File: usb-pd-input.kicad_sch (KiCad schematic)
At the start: 18 parts, among them J1 USB-C, J2 Pogo pads, Q1 -30V -4A, U1 STUSB4500QTR

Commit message: fix: Add missing footprints and LCSC Part numbers to R15, R16, J2
R15/R16: footprint zudo-pd:R0603, LCSC Part C25999 (4.7k 0603 Basic)
J2: footprint zudo-pd:PogoPad_1x04_P2.54mm (no LCSC, bare copper pads)

Co-Authored-By: Claude <noreply@anthropic.com>
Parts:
- J2: footprint (none) -> zudo-pd:PogoPad_1x04_P2.54mm
- R15, R16: footprint (none) -> zudo-pd:R0603; LCSC Part (none) -> C25999
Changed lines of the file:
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@@
 			)
 		)
-		(property "Footprint" ""
+		(property "Footprint" "zudo-pd:PogoPad_1x04_P2.54mm"
 			(at 120.65 127 0)
 			(effects
@@
 			)
 		)
-		(property "Footprint" ""
+		(property "Footprint" "zudo-pd:R0603"
 			(at 126.492 135.89 90)
 			(effects
@@
 		)
 		(property "Description" "Resistor"
+			(at 128.27 135.89 0)
+			(effects
+				(font
+					(size 1.27 1.27)
+				)
+				(hide yes)
+			)
+		)
+		(property "LCSC Part" "C25999"
 			(at 128.27 135.89 0)
 			(effects
@@
 			)
 		)
-		(property "Footprint" ""
+		(property "Footprint" "zudo-pd:R0603"
 			(at 136.652 135.89 90)
 			(effects
@@
 			(at 138.43 135.89 0)
 			(effects
+				(font
+					(size 1.27 1.27)
+				)
+				(hide yes)
+			)
+		)
+		(property "LCSC Part" "C25999"
+			(at 138.43 135.89 0)
+			(effects

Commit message: refactor(hardware): update LCSC part numbers and PCB routing for PCBA v2
- Update capacitor part numbers to JLCPCB-compatible variants
- Standardize LCSC part property naming across schematics
- Adjust PCB routing for improved layout and signal integrity

Co-Authored-By: Claude <noreply@anthropic.com>
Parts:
- C1: LCSC Part C7432781 -> C13585
- C2, C35: LCSC Part C49678 -> C28233
- C30, C34: LCSC Part C6119849 -> C15849
- R11: LCSC Part C14675 -> C25803
- R12: LCSC Part C23168 -> C23206
- R15, R16: LCSC Part C25999 -> C23162
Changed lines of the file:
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@@
 			)
 		)
-		(property "LCSC Part" "C14675"
+		(property "LCSC Part" "C25803"
 			(at 200.66 104.14 0)
 			(effects
@@
 			)
 		)
-		(property "Datasheet" "https://lcsc.com/product-detail/Multilayer-Ceramic-Capacitors-MLCC-SMD-SMT_100nF-104-10-50V_C49678.html"
+		(property "Datasheet" "https://jlcpcb.com/partdetail/C28233"
 			(at 203.2 115.57 0)
 			(effects
@@
 			)
 		)
-		(property "LCSC Part" "C49678"
+		(property "LCSC Part" "C28233"
 			(at 200.66 115.57 0)
 			(effects
@@
 			)
 		)
-		(property "LCSC Part" "C7432781"
+		(property "LCSC Part" "C13585"
 			(at 243.84 21.59 0)
 			(effects
@@
 			)
 		)
-		(property "Datasheet" "https://lcsc.com/product-detail/Multilayer-Ceramic-Capacitors-MLCC-SMD-SMT_100nF-104-10-50V_C49678.html"
+		(property "Datasheet" "https://jlcpcb.com/partdetail/C28233"
 			(at 227.33 21.59 0)
 			(effects
@@
 			)
 		)
-		(property "LCSC Part" "C49678"
+		(property "LCSC Part" "C28233"
 			(at 229.87 21.59 0)
 			(effects
@@
 			)
 		)
-		(property "LCSC Part" "C6119849"
+		(property "LCSC Part" "C15849"
 			(at 217.17 46.99 0)
 			(effects
@@
 			)
 		)
-		(property "LCSC Part" "C25999"
+		(property "LCSC Part" "C23162"
 			(at 128.27 135.89 0)
 			(effects
@@
 			)
 		)
-		(property "LCSC Part" "C25999"
+		(property "LCSC Part" "C23162"
 			(at 138.43 135.89 0)
 			(effects
@@
 			)
 		)
-		(property "LCSC Part" "C23168"
+		(property "LCSC Part" "C23206"
 			(at 209.55 95.25 0)
 			(effects
@@
 			)
 		)
-		(property "LCSC Part" "C6119849"
+		(property "LCSC Part" "C15849"
 			(at 217.17 60.96 0)
 			(effects

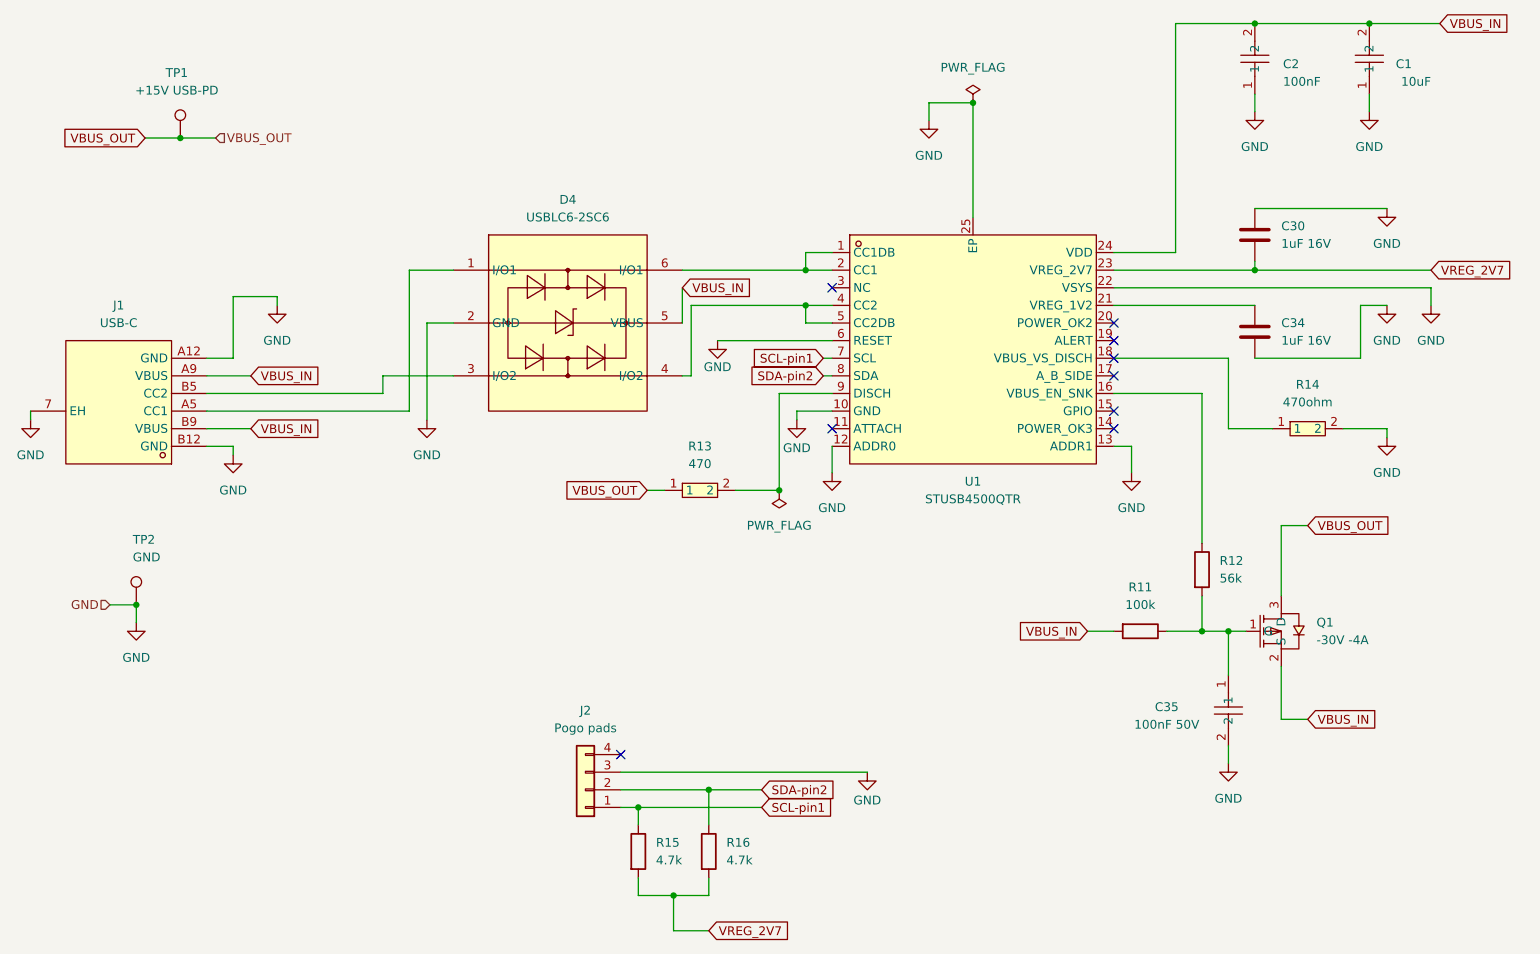
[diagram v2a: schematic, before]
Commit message: feat(hardware): v3 CC pin fix — external 10k Rd on CC1/CC2, CC1DB/CC2DB to GND
Fixed STUSB4500 USB-PD controller issue on v2 PCBAs where CC1DB was internally shorted to GND. Solution: added external 10kΩ pulldown resistors (R17/R18) on CC1/CC2 lines and rerouted U1 pins 1 (CC1DB) and 5 (CC2DB) directly to GND instead of CC1/CC2 nets. Updated BOM with all pulldown entries (R15/R16 existing, R17/R18 new for v3).

Co-Authored-By: Claude <noreply@anthropic.com>
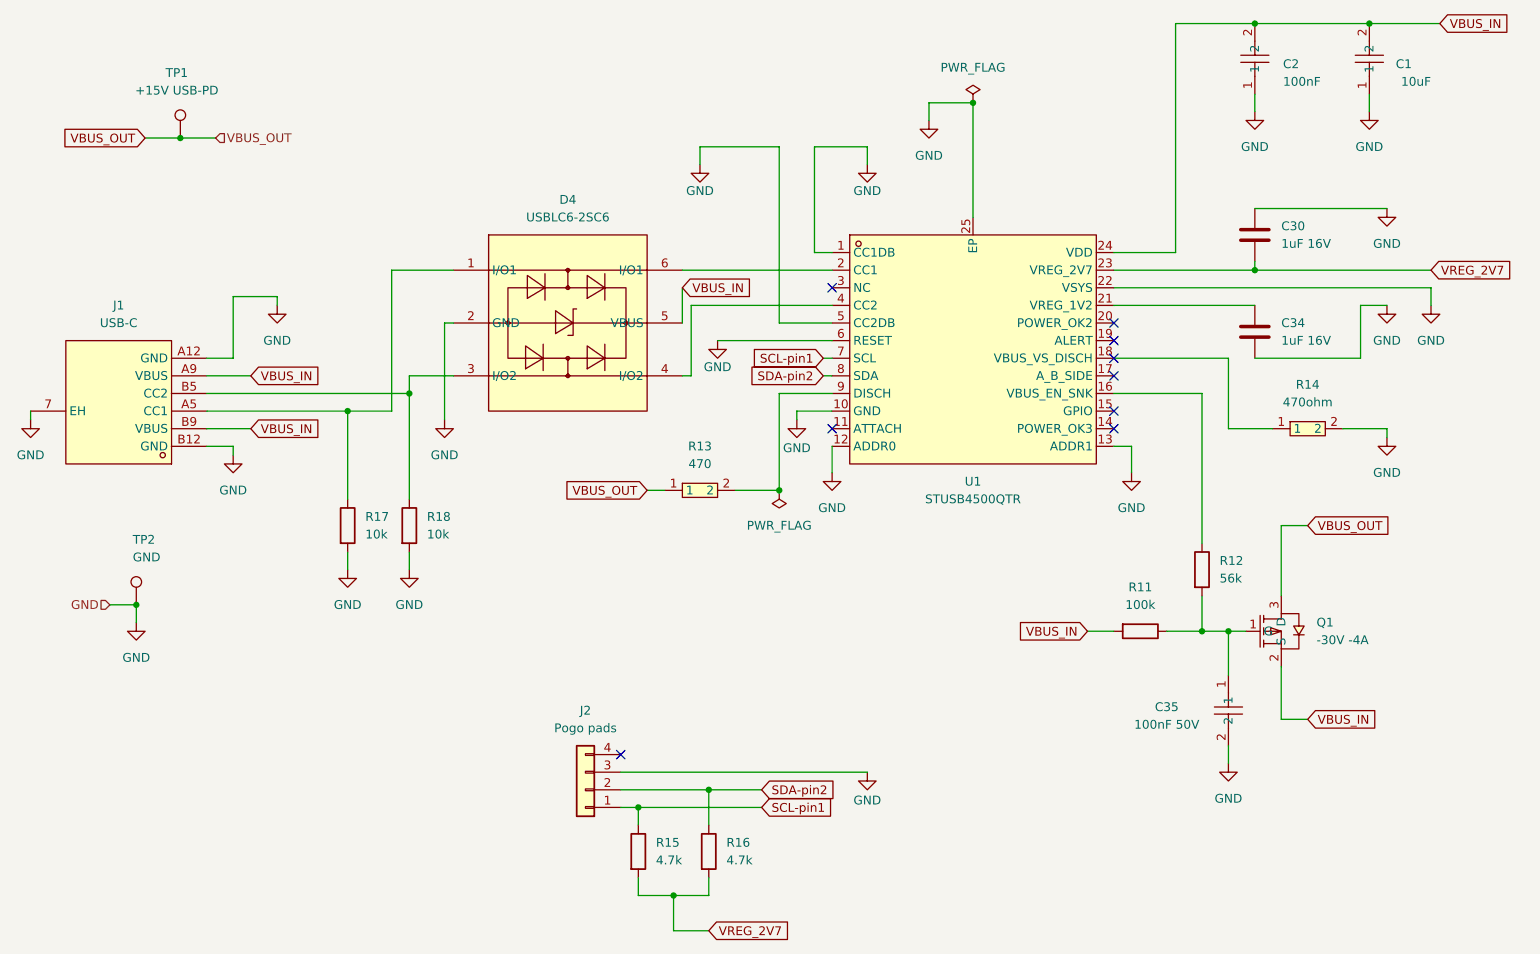
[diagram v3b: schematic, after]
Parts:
- added R17, R18: 10k, zudo-pd:R0603, symbol Device:R
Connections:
- net GND: now also U1.1 (CC1DB), U1.5 (CC2DB), R17.2, R18.2
- net at D4.1 (I/O1), J1.A5 (CC1): now also R17.1
- net at D4.3 (I/O2), J1.B5 (CC2): now also R18.1
- net at D4.6 (I/O1), U1.2 (CC1): no longer U1.1 (CC1DB)
- net at D4.4 (I/O2), U1.4 (CC2): no longer U1.5 (CC2DB)

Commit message: feat(usb-pd): add v3 test point pogo block (J3) + 1x8 pogo footprint
Added a new test point header (J3) with 1x8 pogo pad footprint to enable chip-level
debugging of STUSB4500 signals on v3. Pogo pads allow future signal access without
hot-air rework (the painful v2 workaround). Includes:
- New PogoPad_1x08_P2.54mm footprint for both master and KiCad library copies
- J3 connector wired to key STUSB4500 signals in schematic
- Planning doc (test-points-v3.md) with full signal mapping
- Also bumped R17/R18 values in usb-pd-input.kicad_sch as part of v3 finalization

Co-Authored-By: Claude <noreply@anthropic.com>
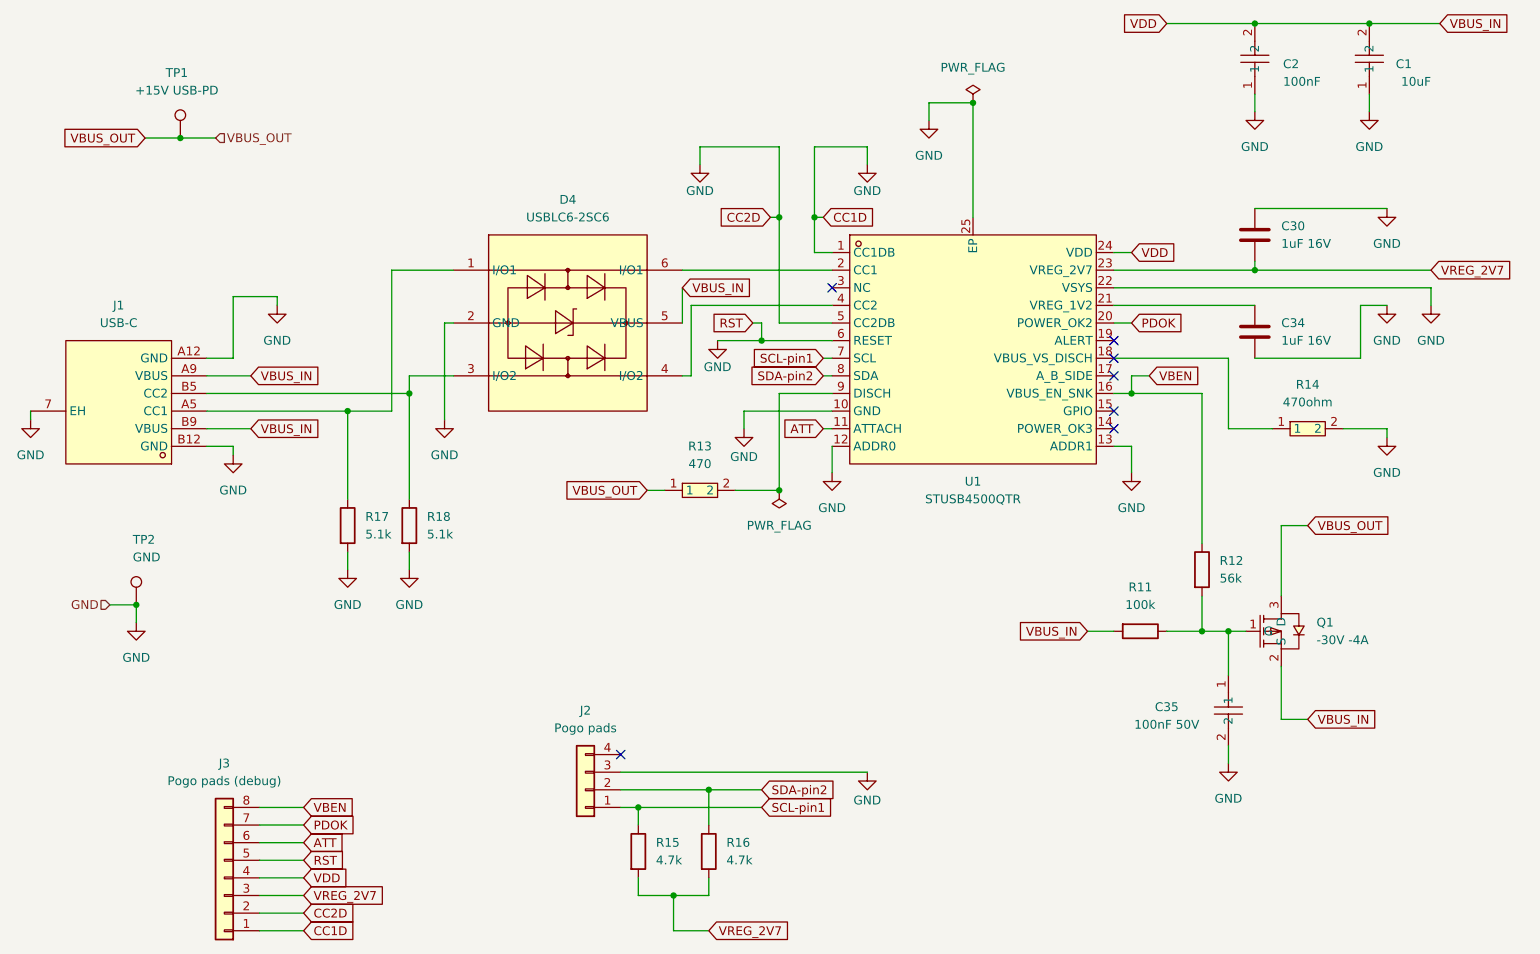
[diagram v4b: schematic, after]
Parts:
- added J3: Pogo pads (debug), zudo-pd:PogoPad_1x08_P2.54mm, symbol Connector_Generic:Conn_01x08
- R17, R18: value 10k -> 5.1k; LCSC Part C25804 -> C23186
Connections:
- net GND: now also J3.1 (Pin_1), J3.2 (Pin_2), J3.5 (Pin_5)
- net VBUS_IN: now also J3.4 (Pin_4)
- net VREG_2V7: now also J3.3 (Pin_3)
- net ATT: now reaches U1.11 (ATTACH)
- net ATT: now also J3.6 (Pin_6)
- net VBEN: now reaches R12.1, U1.16 (VBUS_EN_SNK)
- net VBEN: now also J3.8 (Pin_8)
- net PDOK: now reaches U1.20 (POWER_OK2)
- net PDOK: now also J3.7 (Pin_7)
- no-connect marks 9 -> 7
